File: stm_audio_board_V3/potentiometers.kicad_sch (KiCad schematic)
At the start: 15 parts, among them J14 External_POT

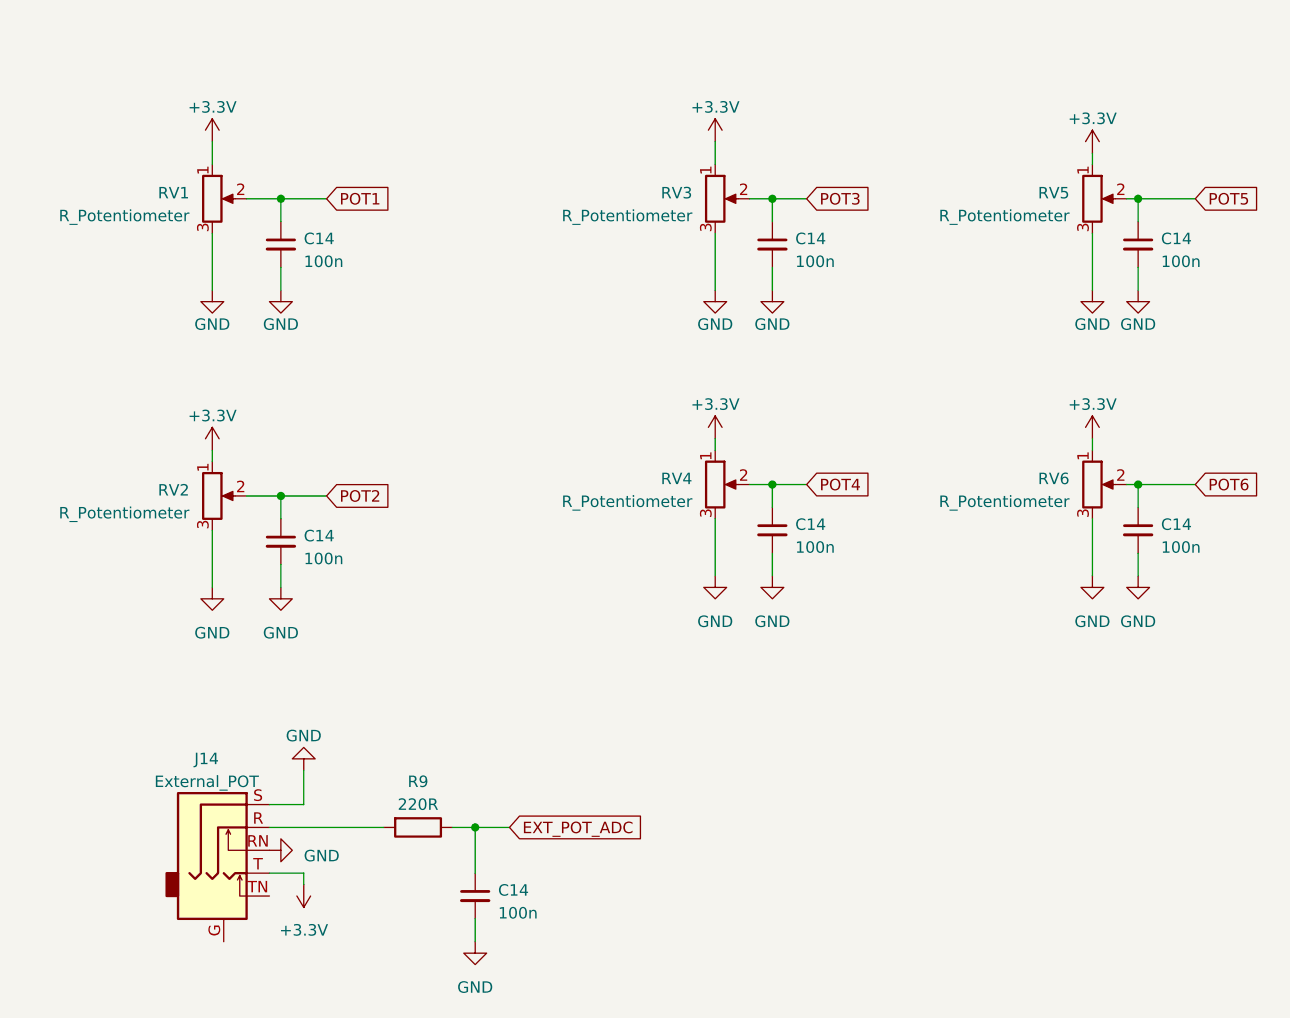
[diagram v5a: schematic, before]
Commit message: minor changes to components
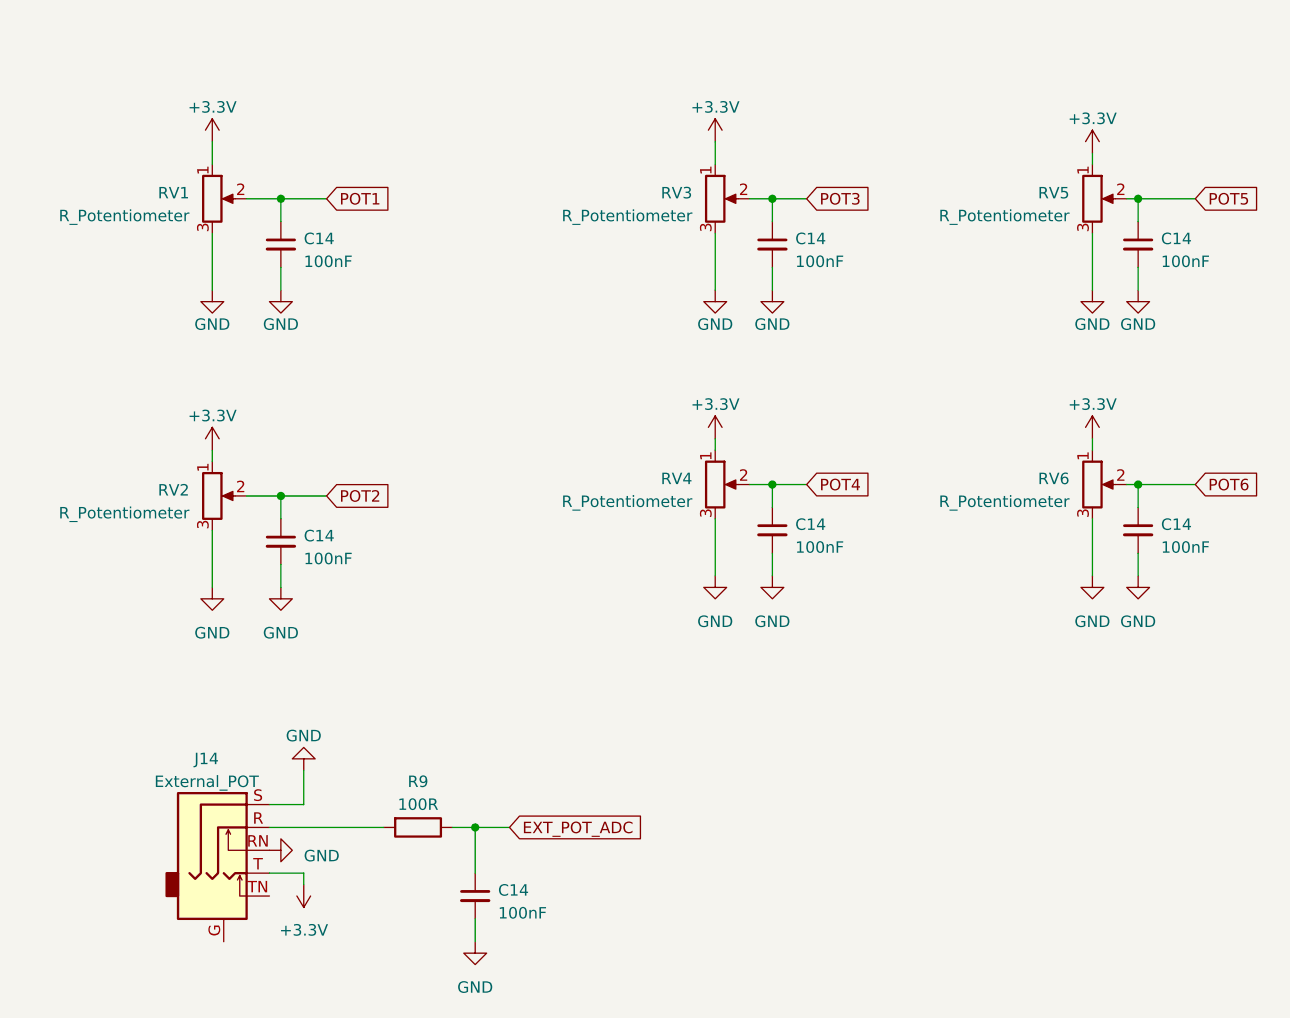
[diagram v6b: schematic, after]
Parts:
- C14: value 100n -> 100nF; JLCPCB (none) -> C14663; LCSC Part (none) -> C14663
- J14: LCSC Part (none) -> C309275
- R9: value 220R -> 100R; JLCPCB (none) -> C22775; LCSC Part (none) -> C22775
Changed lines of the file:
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@@
+      (effects (font (size 1.27 1.27)) hide)
+    )
+    (property "LCSC Part" "" (at 97.79 48.26 0)
       (effects (font (size 1.27 1.27)) hide)
     )
@@
       (effects (font (size 1.27 1.27)) (justify left))
     )
-    (property "Value" "100n" (at 52.07 55.2513 0)
+    (property "Value" "100nF" (at 52.07 55.2513 0)
       (effects (font (size 1.27 1.27)) (justify left))
     )
@@
     )
     (property "Datasheet" "~" (at 49.53 53.34 0)
+      (effects (font (size 1.27 1.27)) hide)
+    )
+    (property "JLCPCB" "C14663" (at 49.53 53.34 0)
+      (effects (font (size 1.27 1.27)) hide)
+    )
+    (property "LCSC Part" "C14663" (at 49.53 53.34 0)
       (effects (font (size 1.27 1.27)) hide)
     )
@@
       (effects (font (size 1.27 1.27)) (justify left))
     )
-    (property "Value" "100n" (at 73.66 127.6413 0)
+    (property "Value" "100nF" (at 73.66 127.6413 0)
       (effects (font (size 1.27 1.27)) (justify left))
     )
@@
     )
     (property "Datasheet" "~" (at 71.12 125.73 0)
+      (effects (font (size 1.27 1.27)) hide)
+    )
+    (property "JLCPCB" "C14663" (at 71.12 125.73 0)
+      (effects (font (size 1.27 1.27)) hide)
+    )
+    (property "LCSC Part" "C14663" (at 71.12 125.73 0)
       (effects (font (size 1.27 1.27)) hide)
     )
@@
       (effects (font (size 1.27 1.27)) (justify left))
     )
-    (property "Value" "100n" (at 106.68 55.2513 0)
+    (property "Value" "100nF" (at 106.68 55.2513 0)
       (effects (font (size 1.27 1.27)) (justify left))
     )
@@
       (effects (font (size 1.27 1.27)) hide)
     )
+    (property "JLCPCB" "C14663" (at 104.14 53.34 0)
+      (effects (font (size 1.27 1.27)) hide)
+    )
+    (property "LCSC Part" "C14663" (at 104.14 53.34 0)
+      (effects (font (size 1.27 1.27)) hide)
+    )
     (pin "1")
     (pin "2")
@@
       (effects (font (size 1.27 1.27)) (justify left))
     )
-    (property "Value" "100n" (at 147.32 87.0013 0)
+    (property "Value" "100nF" (at 147.32 87.0013 0)
       (effects (font (size 1.27 1.27)) (justify left))
     )
@@
     )
     (property "Datasheet" "~" (at 144.78 85.09 0)
+      (effects (font (size 1.27 1.27)) hide)
+    )
+    (property "JLCPCB" "C14663" (at 144.78 85.09 0)
+      (effects (font (size 1.27 1.27)) hide)
+    )
+    (property "LCSC Part" "C14663" (at 144.78 85.09 0)
       (effects (font (size 1.27 1.27)) hide)
     )
@@
       (effects (font (size 1.27 1.27)) (justify left))
     )
-    (property "Value" "100n" (at 52.07 88.2713 0)
+    (property "Value" "100nF" (at 52.07 88.2713 0)
       (effects (font (size 1.27 1.27)) (justify left))
     )
@@
     )
     (property "Datasheet" "~" (at 49.53 86.36 0)
+      (effects (font (size 1.27 1.27)) hide)
+    )
+    (property "JLCPCB" "C14663" (at 49.53 86.36 0)
+      (effects (font (size 1.27 1.27)) hide)
+    )
+    (property "LCSC Part" "C14663" (at 49.53 86.36 0)
       (effects (font (size 1.27 1.27)) hide)
     )
@@
     )
     (property "Datasheet" "~" (at 43.18 118.11 0)
+      (effects (font (size 1.27 1.27)) hide)
+    )
+    (property "LCSC Part" "C309275" (at 43.18 118.11 0)
       (effects (font (size 1.27 1.27)) hide)
     )
@@
       (effects (font (size 1.27 1.27)) hide)
     )
+    (property "LCSC Part" "" (at 139.7 80.01 0)
+      (effects (font (size 1.27 1.27)) hide)
+    )
     (pin "1")
     (pin "2")
@@
     )
     (property "Field5" "" (at 41.91 48.26 0)
+      (effects (font (size 1.27 1.27)) hide)
+    )
+    (property "LCSC Part" "" (at 41.91 48.26 0)
       (effects (font (size 1.27 1.27)) hide)
     )
@@
       (effects (font (size 1.27 1.27)) hide)
     )
+    (property "LCSC Part" "" (at 139.7 48.26 0)
+      (effects (font (size 1.27 1.27)) hide)
+    )
     (pin "1")
     (pin "2")
@@
       (effects (font (size 1.27 1.27)))
     )
-    (property "Value" "220R" (at 64.77 115.57 90)
+    (property "Value" "100R" (at 64.77 115.57 90)
       (effects (font (size 1.27 1.27)))
     )
@@
     )
     (property "Datasheet" "~" (at 64.77 118.11 0)
+      (effects (font (size 1.27 1.27)) hide)
+    )
+    (property "JLCPCB" "C22775" (at 64.77 118.11 0)
+      (effects (font (size 1.27 1.27)) hide)
+    )
+    (property "LCSC Part" "C22775" (at 64.77 118.11 0)
       (effects (font (size 1.27 1.27)) hide)
     )
@@
       (effects (font (size 1.27 1.27)) (justify left))
     )
-    (property "Value" "100n" (at 106.68 87.0013 0)
+    (property "Value" "100nF" (at 106.68 87.0013 0)
       (effects (font (size 1.27 1.27)) (justify left))
     )
@@
     )
     (property "Datasheet" "~" (at 104.14 85.09 0)
+      (effects (font (size 1.27 1.27)) hide)
+    )
+    (property "JLCPCB" "C14663" (at 104.14 85.09 0)
+      (effects (font (size 1.27 1.27)) hide)
+    )
+    (property "LCSC Part" "C14663" (at 104.14 85.09 0)
       (effects (font (size 1.27 1.27)) hide)
     )
@@
     )
     (property "Field5" "" (at 97.79 80.01 0)
+      (effects (font (size 1.27 1.27)) hide)
+    )
+    (property "LCSC Part" "" (at 97.79 80.01 0)
       (effects (font (size 1.27 1.27)) hide)
     )
@@
       (effects (font (size 1.27 1.27)) (justify left))
     )
-    (property "Value" "100n" (at 147.32 55.2513 0)
+    (property "Value" "100nF" (at 147.32 55.2513 0)
       (effects (font (size 1.27 1.27)) (justify left))
     )
@@
     )
     (property "Datasheet" "~" (at 144.78 53.34 0)
+      (effects (font (size 1.27 1.27)) hide)
+    )
+    (property "JLCPCB" "C14663" (at 144.78 53.34 0)
+      (effects (font (size 1.27 1.27)) hide)
+    )
+    (property "LCSC Part" "C14663" (at 144.78 53.34 0)
       (effects (font (size 1.27 1.27)) hide)
     )
@@
       (effects (font (size 1.27 1.27)) hide)
     )
+    (property "LCSC Part" "" (at 41.91 81.28 0)
+      (effects (font (size 1.27 1.27)) hide)
+    )

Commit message: added silkscreen captions, capacitor between gnd and earth
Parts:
- J14: footprint Connector_Audio:Jack_6.35mm_Neutrik_NMJ6HCD2_Horizontal -> stm_audio_board_footprints:6.3_jack_new_ref; LCSC Part C309275 -> C309277
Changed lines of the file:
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@@
       (effects (font (size 1.27 1.27)))
     )
-    (property "Footprint" "Connector_Audio:Jack_6.35mm_Neutrik_NMJ6HCD2_Horizontal" (at 43.18 118.11 0)
+    (property "Footprint" "stm_audio_board_footprints:6.3_jack_new_ref" (at 43.18 118.11 0)
       (effects (font (size 1.27 1.27)) hide)
     )
@@
       (effects (font (size 1.27 1.27)) hide)
     )
-    (property "LCSC Part" "C309275" (at 43.18 118.11 0)
+    (property "LCSC Part" "C309277" (at 43.18 118.11 0)
       (effects (font (size 1.27 1.27)) hide)
     )
